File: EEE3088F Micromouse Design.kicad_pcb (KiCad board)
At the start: 2 copper layers, 74.5 x 78.2 mm, 4 parts, among them J1 Conn_02x16_Odd_Even, J2 Conn_01x02, U1 INA219AxD

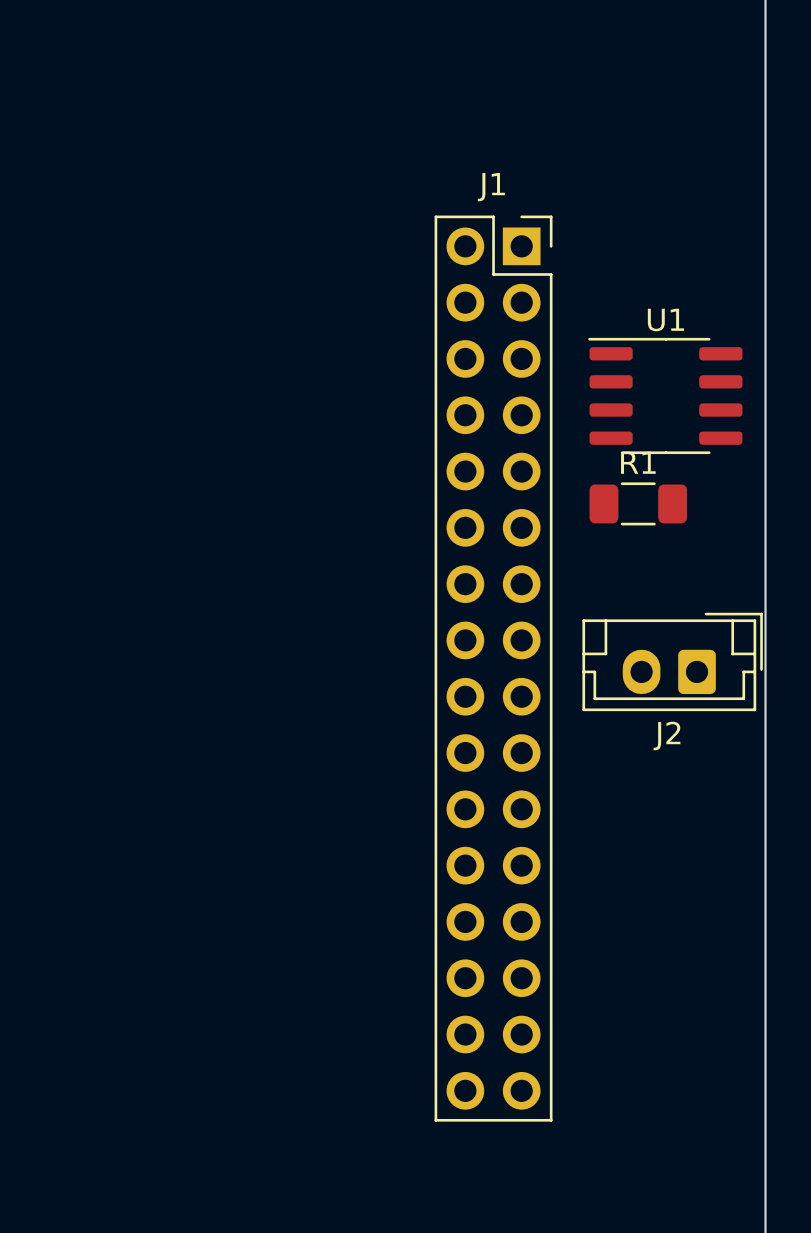
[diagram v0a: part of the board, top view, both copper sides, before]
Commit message: Added DRV8837 Motor Driver x4. Footprint PCB Organisation outstanding
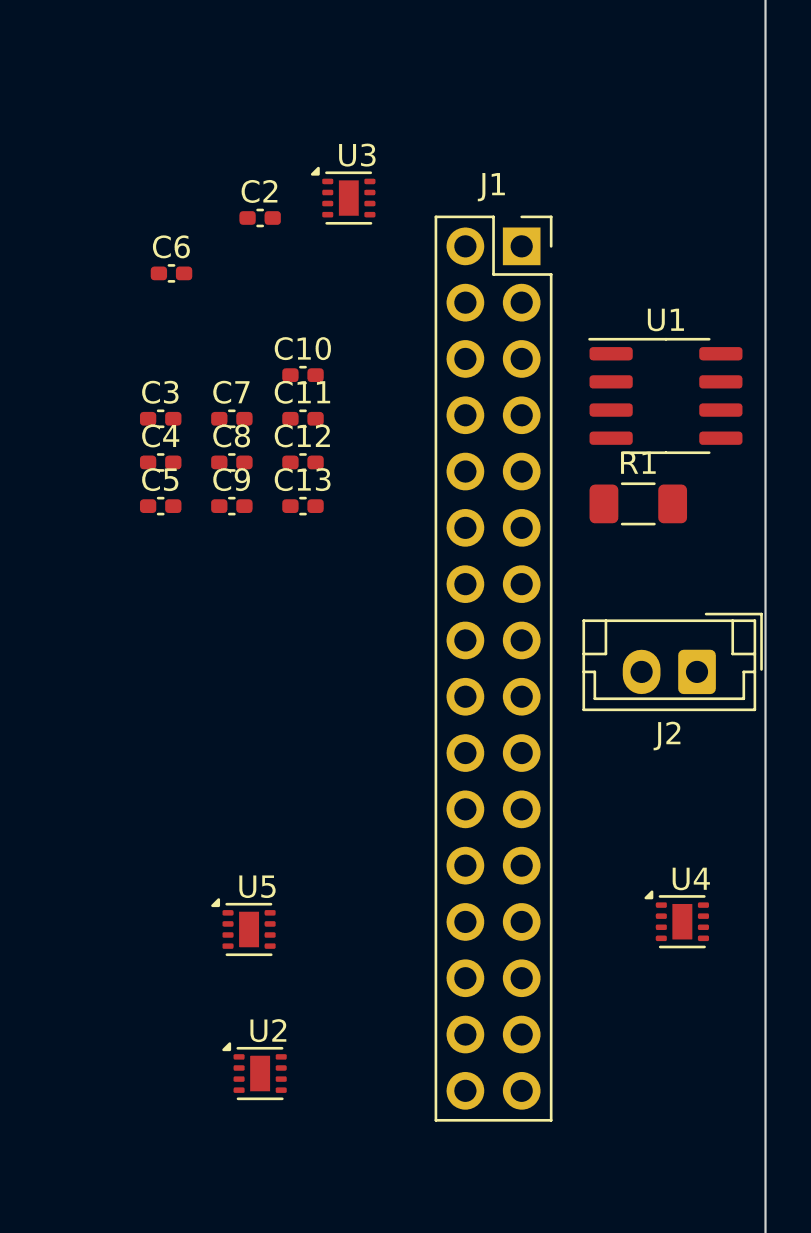
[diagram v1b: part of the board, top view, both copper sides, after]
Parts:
- added C10: 0.1mF, Capacitor_SMD:C_0402_1005Metric_Pad0.74x0.62mm_HandSolder, F.Cu at (93.4, 80.6)
- added C11: 0.1mF, Capacitor_SMD:C_0402_1005Metric_Pad0.74x0.62mm_HandSolder, F.Cu at (93.4, 82.6)
- added C12: 0.1mF, Capacitor_SMD:C_0402_1005Metric_Pad0.74x0.62mm_HandSolder, F.Cu at (93.4, 84.5)
- added C13: 0.1mF, Capacitor_SMD:C_0402_1005Metric_Pad0.74x0.62mm_HandSolder, F.Cu at (93.4, 86.5)
- added C2: 0.1mF, Capacitor_SMD:C_0402_1005Metric_Pad0.74x0.62mm_HandSolder, F.Cu at (91.5, 73.5)
- added C3: 0.1mF, Capacitor_SMD:C_0402_1005Metric_Pad0.74x0.62mm_HandSolder, F.Cu at (87.0, 82.6)
- added C4: 0.1mF, Capacitor_SMD:C_0402_1005Metric_Pad0.74x0.62mm_HandSolder, F.Cu at (87.0, 84.5)
- added C5: 0.1mF, Capacitor_SMD:C_0402_1005Metric_Pad0.74x0.62mm_HandSolder, F.Cu at (87.0, 86.5)
- added C6: 0.1mF, Capacitor_SMD:C_0402_1005Metric_Pad0.74x0.62mm_HandSolder, F.Cu at (87.5, 76.0)
- added C7: 0.1mF, Capacitor_SMD:C_0402_1005Metric_Pad0.74x0.62mm_HandSolder, F.Cu at (90.2, 82.6)
- added C8: 0.1mF, Capacitor_SMD:C_0402_1005Metric_Pad0.74x0.62mm_HandSolder, F.Cu at (90.2, 84.5)
- added C9: 0.1mF, Capacitor_SMD:C_0402_1005Metric_Pad0.74x0.62mm_HandSolder, F.Cu at (90.2, 86.5)
- added U2: DRV8837, Package_SON:WSON-8-1EP_2x2mm_P0.5mm_EP0.9x1.6mm, F.Cu at (91.5, 112.1)
- added U3: DRV8837, Package_SON:WSON-8-1EP_2x2mm_P0.5mm_EP0.9x1.6mm, F.Cu at (95.5, 72.6)
- added U4: DRV8837, Package_SON:WSON-8-1EP_2x2mm_P0.5mm_EP0.9x1.6mm, F.Cu at (110.5, 105.2)
- added U5: DRV8837, Package_SON:WSON-8-1EP_2x2mm_P0.5mm_EP0.9x1.6mm, F.Cu at (91.0, 105.6)
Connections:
- J1 pad 1: unconnected-(J1-Pin_1-Pad1) -> /Motor2_B_OUT
- J1 pad 10: unconnected-(J1-Pin_10-Pad10) -> /MOTOR4_CTRL2
- J1 pad 2: unconnected-(J1-Pin_2-Pad2) -> /Motor2_A_OUT
- J1 pad 20: unconnected-(J1-Pin_20-Pad20) -> /5V Out
- J1 pad 24: unconnected-(J1-Pin_24-Pad24) -> /MOTOR3_CTRL1
- J1 pad 26: unconnected-(J1-Pin_26-Pad26) -> /MOTOR3_CTRL2
- J1 pad 27: unconnected-(J1-Pin_27-Pad27) -> /MOTOR3_A_OUT
- J1 pad 28: unconnected-(J1-Pin_28-Pad28) -> /MOTOR1_CTRL1
- J1 pad 29: unconnected-(J1-Pin_29-Pad29) -> /MOTOR3_B_OUT
- J1 pad 3: unconnected-(J1-Pin_3-Pad3) -> /Motor4_A_OUT
- J1 pad 30: unconnected-(J1-Pin_30-Pad30) -> /MOTOR1_CTRL2
- J1 pad 31: unconnected-(J1-Pin_31-Pad31) -> /MOTOR1_B_OUT
- J1 pad 32: unconnected-(J1-Pin_32-Pad32) -> /MOTOR1_A_OUT
- J1 pad 4: unconnected-(J1-Pin_4-Pad4) -> /MOTOR2_CTRL1
- J1 pad 5: unconnected-(J1-Pin_5-Pad5) -> /Motor4_B_OUT
- J1 pad 6: unconnected-(J1-Pin_6-Pad6) -> /MOTOR2_CTRL2
- J1 pad 8: unconnected-(J1-Pin_8-Pad8) -> /MOTOR4_CTRL1

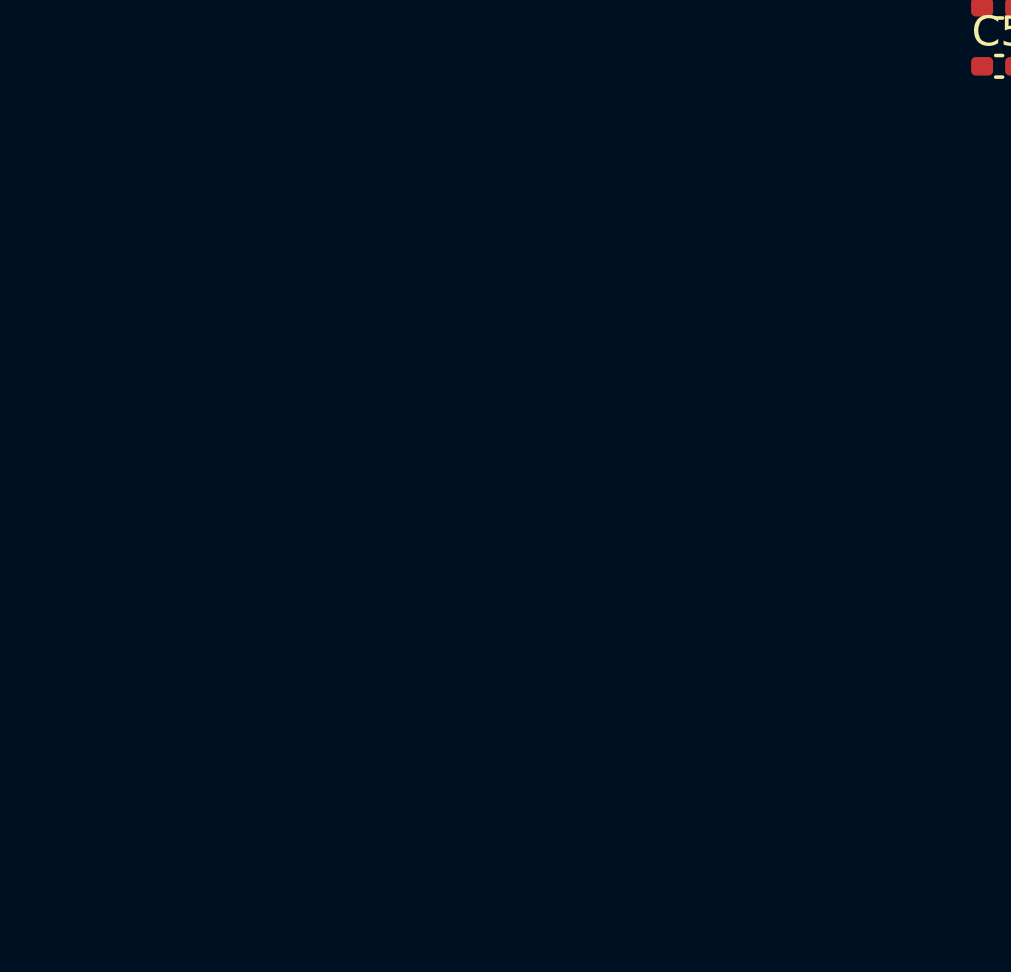
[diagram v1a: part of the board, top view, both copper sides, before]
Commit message: Added the Battery Charging Circuit
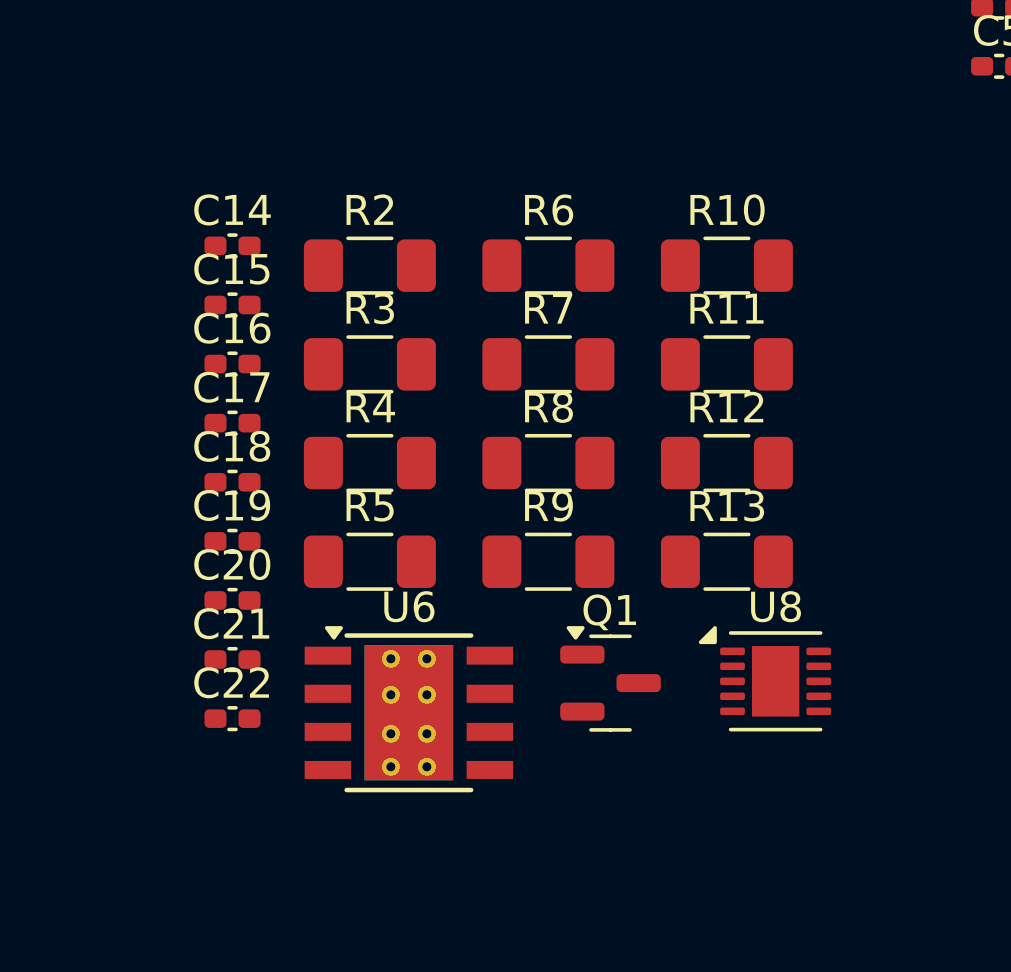
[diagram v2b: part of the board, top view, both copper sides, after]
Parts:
- added C14: 0.1mF, Capacitor_SMD:C_0402_1005Metric_Pad0.74x0.62mm_HandSolder, F.Cu at (61.5, 92.5)
- added C15: 10uF, Capacitor_SMD:C_0402_1005Metric_Pad0.74x0.62mm_HandSolder, F.Cu at (61.5, 94.5)
- added C16: 0.1uF, Capacitor_SMD:C_0402_1005Metric_Pad0.74x0.62mm_HandSolder, F.Cu at (61.5, 96.4)
- added C17: 0.1uF, Capacitor_SMD:C_0402_1005Metric_Pad0.74x0.62mm_HandSolder, F.Cu at (61.5, 98.4)
- added C18: 47nF, Capacitor_SMD:C_0402_1005Metric_Pad0.74x0.62mm_HandSolder, F.Cu at (61.5, 100.4)
- added C19: 22pF, Capacitor_SMD:C_0402_1005Metric_Pad0.74x0.62mm_HandSolder, F.Cu at (61.5, 102.3)
- added C20: 22uF, Capacitor_SMD:C_0402_1005Metric_Pad0.74x0.62mm_HandSolder, F.Cu at (61.5, 104.3)
- added C21: 22uF, Capacitor_SMD:C_0402_1005Metric_Pad0.74x0.62mm_HandSolder, F.Cu at (61.5, 106.3)
- added C22: 22uF, Capacitor_SMD:C_0402_1005Metric_Pad0.74x0.62mm_HandSolder, F.Cu at (61.5, 108.2)
- added Q1: AO3400A, Package_TO_SOT_SMD:SOT-23, F.Cu at (74.1, 107.1)
- added R10: 330, Resistor_SMD:R_1206_3216Metric_Pad1.30x1.75mm_HandSolder, F.Cu at (77.9, 93.1)
- added R11: 2.2k, Resistor_SMD:R_1206_3216Metric_Pad1.30x1.75mm_HandSolder, F.Cu at (77.9, 96.4)
- added R12: 270, Resistor_SMD:R_1206_3216Metric_Pad1.30x1.75mm_HandSolder, F.Cu at (77.9, 99.7)
- added R13: 10k, Resistor_SMD:R_1206_3216Metric_Pad1.30x1.75mm_HandSolder, F.Cu at (77.9, 103.0)
- added R2: 5.6k, Resistor_SMD:R_1206_3216Metric_Pad1.30x1.75mm_HandSolder, F.Cu at (66.0, 93.1)
- added R3: 3.3k, Resistor_SMD:R_1206_3216Metric_Pad1.30x1.75mm_HandSolder, F.Cu at (66.0, 96.4)
- added R4: 255k, Resistor_SMD:R_1206_3216Metric_Pad1.30x1.75mm_HandSolder, F.Cu at (66.0, 99.7)
- added R5: 100k, Resistor_SMD:R_1206_3216Metric_Pad1.30x1.75mm_HandSolder, F.Cu at (66.0, 103.0)
- added R6: 10k, Resistor_SMD:R_1206_3216Metric_Pad1.30x1.75mm_HandSolder, F.Cu at (72.0, 93.1)
- added R7: 47k, Resistor_SMD:R_1206_3216Metric_Pad1.30x1.75mm_HandSolder, F.Cu at (72.0, 96.4)
- added R8: 150k, Resistor_SMD:R_1206_3216Metric_Pad1.30x1.75mm_HandSolder, F.Cu at (72.0, 99.7)
- added R9: 4.7k, Resistor_SMD:R_1206_3216Metric_Pad1.30x1.75mm_HandSolder, F.Cu at (72.0, 103.0)
- added U6: TPS5430DDA, Package_SO:TI_SO-PowerPAD-8_ThermalVias, F.Cu at (67.3, 108.0)
- added U8: MCP73833-xxx-MF, Package_DFN_QFN:DFN-10-1EP_3x3mm_P0.5mm_EP1.58x2.35mm, F.Cu at (79.6, 107.0)
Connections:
- J1 pad 13: unconnected-(J1-Pin_13-Pad13) -> /FAST_CHARGE_CTRL
- J1 pad 18: unconnected-(J1-Pin_18-Pad18) -> /3.3V Out

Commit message: Added items to BOM. Need to finish assignment
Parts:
- removed C10, C11, C12, C13, C2, C3, C4, C5, C6, C7, C8, C9: 0.1mF, Capacitor_SMD:C_0402_1005Metric_Pad0.74x0.62mm_HandSolder
- removed Q1: AO3400A, Package_TO_SOT_SMD:SOT-23
- removed R10: 330, Resistor_SMD:R_1206_3216Metric_Pad1.30x1.75mm_HandSolder
- removed R11: 2.2k, Resistor_SMD:R_1206_3216Metric_Pad1.30x1.75mm_HandSolder
- removed R12: 270, Resistor_SMD:R_1206_3216Metric_Pad1.30x1.75mm_HandSolder
- removed R13: 10k, Resistor_SMD:R_1206_3216Metric_Pad1.30x1.75mm_HandSolder
- removed R9: 4.7k, Resistor_SMD:R_1206_3216Metric_Pad1.30x1.75mm_HandSolder
- removed U2, U3, U4, U5: DRV8837, Package_SON:WSON-8-1EP_2x2mm_P0.5mm_EP0.9x1.6mm
- removed U8: MCP73833-xxx-MF, Package_DFN_QFN:DFN-10-1EP_3x3mm_P0.5mm_EP1.58x2.35mm
- added C24: 1uF, Capacitor_SMD:C_0402_1005Metric_Pad0.74x0.62mm_HandSolder, F.Cu at (68.7, 84.0)
- added C33: 1μF, Capacitor_SMD:C_1206_3216Metric_Pad1.33x1.80mm_HandSolder, F.Cu at (73.3, 60.3)
- added C34: 1μF, Capacitor_SMD:C_1206_3216Metric_Pad1.33x1.80mm_HandSolder, F.Cu at (73.3, 63.7)
- added C35: 1μF, Capacitor_SMD:C_1206_3216Metric_Pad1.33x1.80mm_HandSolder, F.Cu at (73.3, 67.0)
- added C36: 1nF, Capacitor_SMD:C_1206_3216Metric_Pad1.33x1.80mm_HandSolder, F.Cu at (73.3, 70.4)
- added C37: 1μF, Capacitor_SMD:C_1206_3216Metric_Pad1.33x1.80mm_HandSolder, F.Cu at (73.3, 73.7)
- added C38: 1nF, Capacitor_SMD:C_1206_3216Metric_Pad1.33x1.80mm_HandSolder, F.Cu at (73.3, 77.1)
- added Q2: AO3400A, Package_TO_SOT_SMD:SOT-23, F.Cu at (65.2, 80.8)
- added R14: 10k, Resistor_SMD:R_1206_3216Metric_Pad1.30x1.75mm_HandSolder, F.Cu at (61.4, 60.3)
- added R15: 1k, Resistor_SMD:R_1206_3216Metric_Pad1.30x1.75mm_HandSolder, F.Cu at (61.4, 63.6)
- added R16: 6.8k, Resistor_SMD:R_1206_3216Metric_Pad1.30x1.75mm_HandSolder, F.Cu at (61.4, 66.9)
- added R21: 33k, Resistor_SMD:R_1206_3216Metric_Pad1.30x1.75mm_HandSolder, F.Cu at (61.4, 70.2)
- added R22: 10k, Resistor_SMD:R_1206_3216Metric_Pad1.30x1.75mm_HandSolder, F.Cu at (61.4, 73.4)
- added R25: 1, Resistor_SMD:R_1206_3216Metric_Pad1.30x1.75mm_HandSolder, F.Cu at (61.4, 76.7)
- added R26: 1, Resistor_SMD:R_1206_3216Metric_Pad1.30x1.75mm_HandSolder, F.Cu at (67.3, 60.3)
- added R27: 4.7k, Resistor_SMD:R_1206_3216Metric_Pad1.30x1.75mm_HandSolder, F.Cu at (67.3, 63.6)
- added R28: 330, Resistor_SMD:R_1206_3216Metric_Pad1.30x1.75mm_HandSolder, F.Cu at (67.3, 66.9)
- added R29: 0.82, Resistor_SMD:R_0603_1608Metric_Pad0.98x0.95mm_HandSolder, F.Cu at (60.6, 79.6)
- added R30: 0.82, Resistor_SMD:R_0603_1608Metric_Pad0.98x0.95mm_HandSolder, F.Cu at (60.6, 82.1)
- added R31: 0.82, Resistor_SMD:R_0603_1608Metric_Pad0.98x0.95mm_HandSolder, F.Cu at (60.6, 84.7)
- added R32: 0.82, Resistor_SMD:R_0603_1608Metric_Pad0.98x0.95mm_HandSolder, F.Cu at (60.6, 87.2)
- added R33: 2.2k, Resistor_SMD:R_1206_3216Metric_Pad1.30x1.75mm_HandSolder, F.Cu at (67.3, 70.2)
- added R34: 270, Resistor_SMD:R_1206_3216Metric_Pad1.30x1.75mm_HandSolder, F.Cu at (67.3, 73.4)
- added U11: DRV8833PW, Package_SO:TSSOP-16_4.4x5mm_P0.65mm, F.Cu at (81.1, 61.9)
- added U12: DRV8833PW, Package_SO:TSSOP-16_4.4x5mm_P0.65mm, F.Cu at (81.1, 68.5)
- added U13: AP22966DC8-7, AP22966DC8-7:IC_AP22966DC8-7, F.Cu at (65.2, 85.3)
- added U15: TP4056-42-ESOP8, Package_SO:SOIC-8-1EP_3.9x4.9mm_P1.27mm_EP2.41x3.3mm_ThermalVias, F.Cu at (74.5, 82.1)
- added U9: CH224K, Package_SO:SSOP-10-1EP_3.9x4.9mm_P1mm_EP2.1x3.3mm, F.Cu at (80.6, 75.3)
- C14: value 0.1mF -> 0.01uF
- R1: value 0.15 -> 0.1
- R4: value 255k -> 220k
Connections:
- net /3.3V Out renamed /3V3 Out
- J1 pad 11: unconnected-(J1-Pin_11-Pad11) -> /EXT_LOAD2_OUT
- J1 pad 14: unconnected-(J1-Pin_14-Pad14) -> /V_Battery+
- J1 pad 19: unconnected-(J1-Pin_19-Pad19) -> GND
- J1 pad 21: unconnected-(J1-Pin_21-Pad21) -> /EXT_LOAD1_OUT
- J1 pad 22: unconnected-(J1-Pin_22-Pad22) -> /HV
- J1 pad 23: unconnected-(J1-Pin_23-Pad23) -> GND
- J1 pad 25: unconnected-(J1-Pin_25-Pad25) -> /CTRL_EXT_LOAD1
- J1 pad 7: unconnected-(J1-Pin_7-Pad7) -> /CTRL_EXT_LOAD2
- R1 pad 1: /Vcc -> Net-(SW1-B)
- R4 pad 2: Net-(U7-SW_4) -> Net-(R21-Pad2)
- R7 pad 2: GND -> /FB
- R8 pad 1: GND -> /FB
- U1 pad 7: /Vcc -> Net-(SW1-B)

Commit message: Adding JLC part numbers
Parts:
- C19: value 22pF -> 1.5nF
- R6: value 10k -> 68k
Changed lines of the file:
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@@
 			)
 		)
+		(property "LCSC" "C25466"
+			(at 0 0 0)
+			(layer "F.SilkS")
+			(hide yes)
+			(effects
+				(font
+					(size 1.27 1.27)
+					(thickness 0.15)
+				)
+			)
+		)
 		(property ki_fp_filters "R_*")
 		(sheetname "/")
@@
 			)
 		)
-		(property "Value" "10k"
+		(property "Value" "68k"
 			(at 0 1.82 0)
 			(layer "F.Fab")
@@
 			)
 		)
+		(property "LCSC" "C970725"
+			(at 0 0 0)
+			(layer "F.SilkS")
+			(hide yes)
+			(effects
+				(font
+					(size 1.27 1.27)
+					(thickness 0.15)
+				)
+			)
+		)
 		(property ki_fp_filters "SSOP*3.9x4.9mm*P1mm*EP2.1x3.3mm*")
 		(sheetname "/")
@@
 			)
 		)
-		(property "Value" "22pF"
+		(property "Value" "1.5nF"
 			(at 0 1.16 0)
 			(layer "F.Fab")
@@
 		(sheetname "/")
 		(sheetfile "EEE3088F Micromouse Design.kicad_sch")
-		(attr through_hole)
+		(attr through_hole dnp)
 		(fp_line
 			(start -3.87 -1.33)
@@
 			)
 		)
+		(property "LCSC" "C87469"
+			(at 0 0 0)
+			(layer "F.SilkS")
+			(hide yes)
+			(effects
+				(font
+					(size 1.27 1.27)
+					(thickness 0.15)
+				)
+			)
+		)
 		(property ki_fp_filters "SOIC*3.9x4.9mm*P1.27mm*")
 		(sheetname "/")
@@
 		(sheetname "/")
 		(sheetfile "EEE3088F Micromouse Design.kicad_sch")
-		(attr through_hole)
+		(attr through_hole dnp)
 		(fp_line
 			(start 5.11 2.31)
@@
 			(hide yes)
 			(effects
+				(font
+					(size 1.27 1.27)
+					(thickness 0.15)
+				)
+			)
+		)
+		(property "LCSC" "C9864"
+			(at 0 0 0)
+			(layer "F.SilkS")
+			(hide yes)
+			(effects
